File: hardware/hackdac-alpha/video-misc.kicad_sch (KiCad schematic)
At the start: 43 parts, among them J2 TTL SYNC, J3 SYNC OUT, P1 BANK2_AUX, Q1 2N7002, Q2 BC847, Q3 BC857, Q4 BC857, U5 MCP47FEB22A1-E/ST, U6 74LVCH16T245, U7 74LVC1G125, X1 ECS-5032MV-270-CN-TR

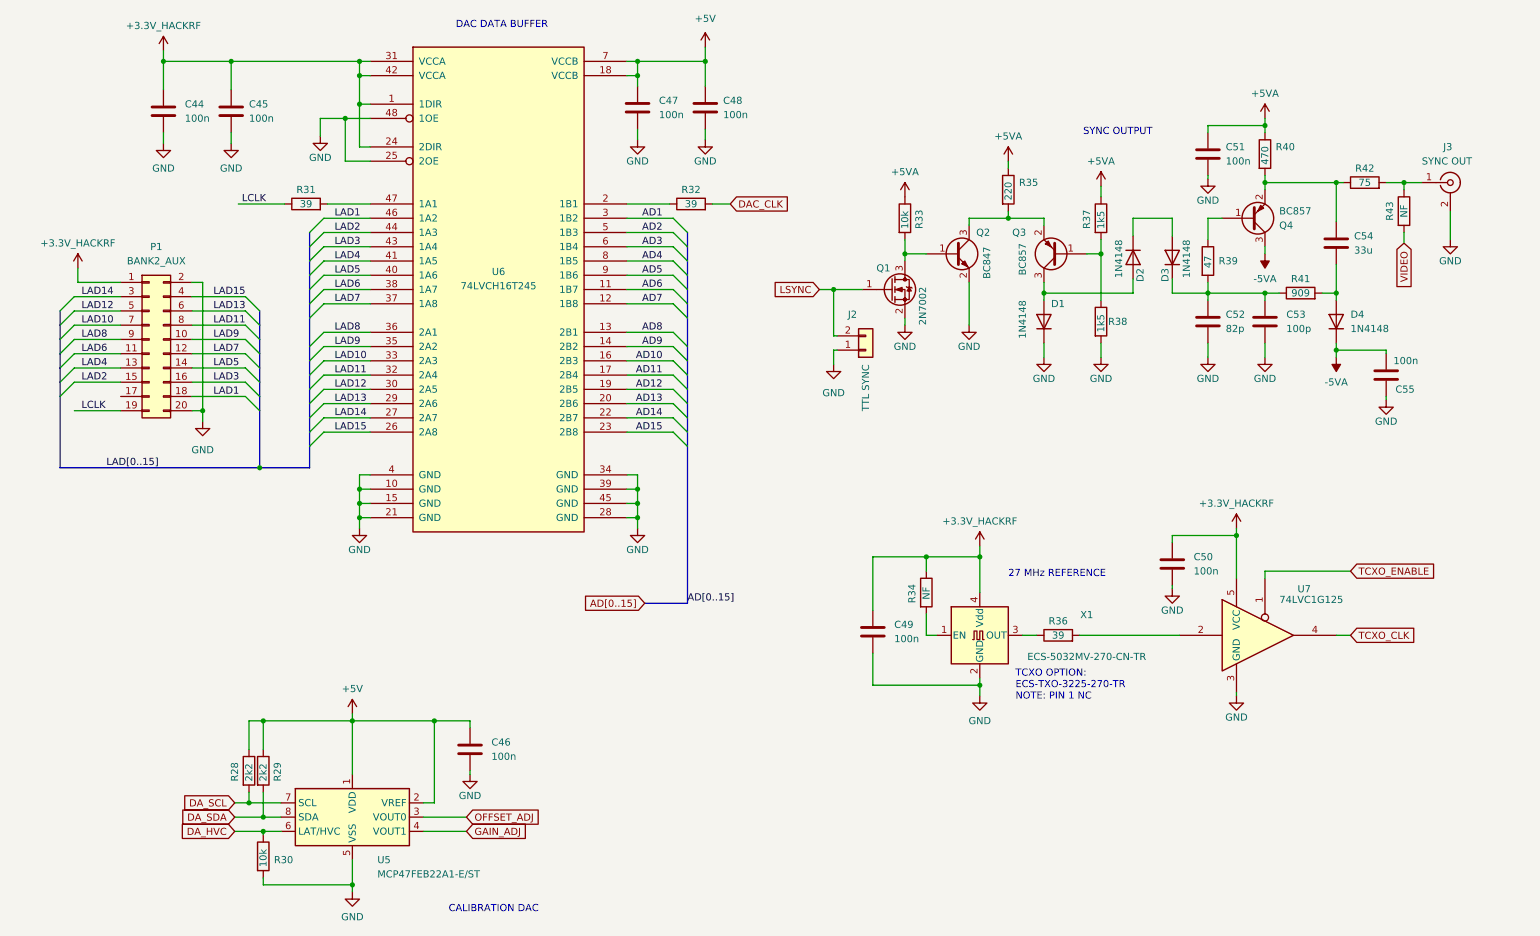
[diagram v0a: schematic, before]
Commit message: Add jumper to configure sync out connector
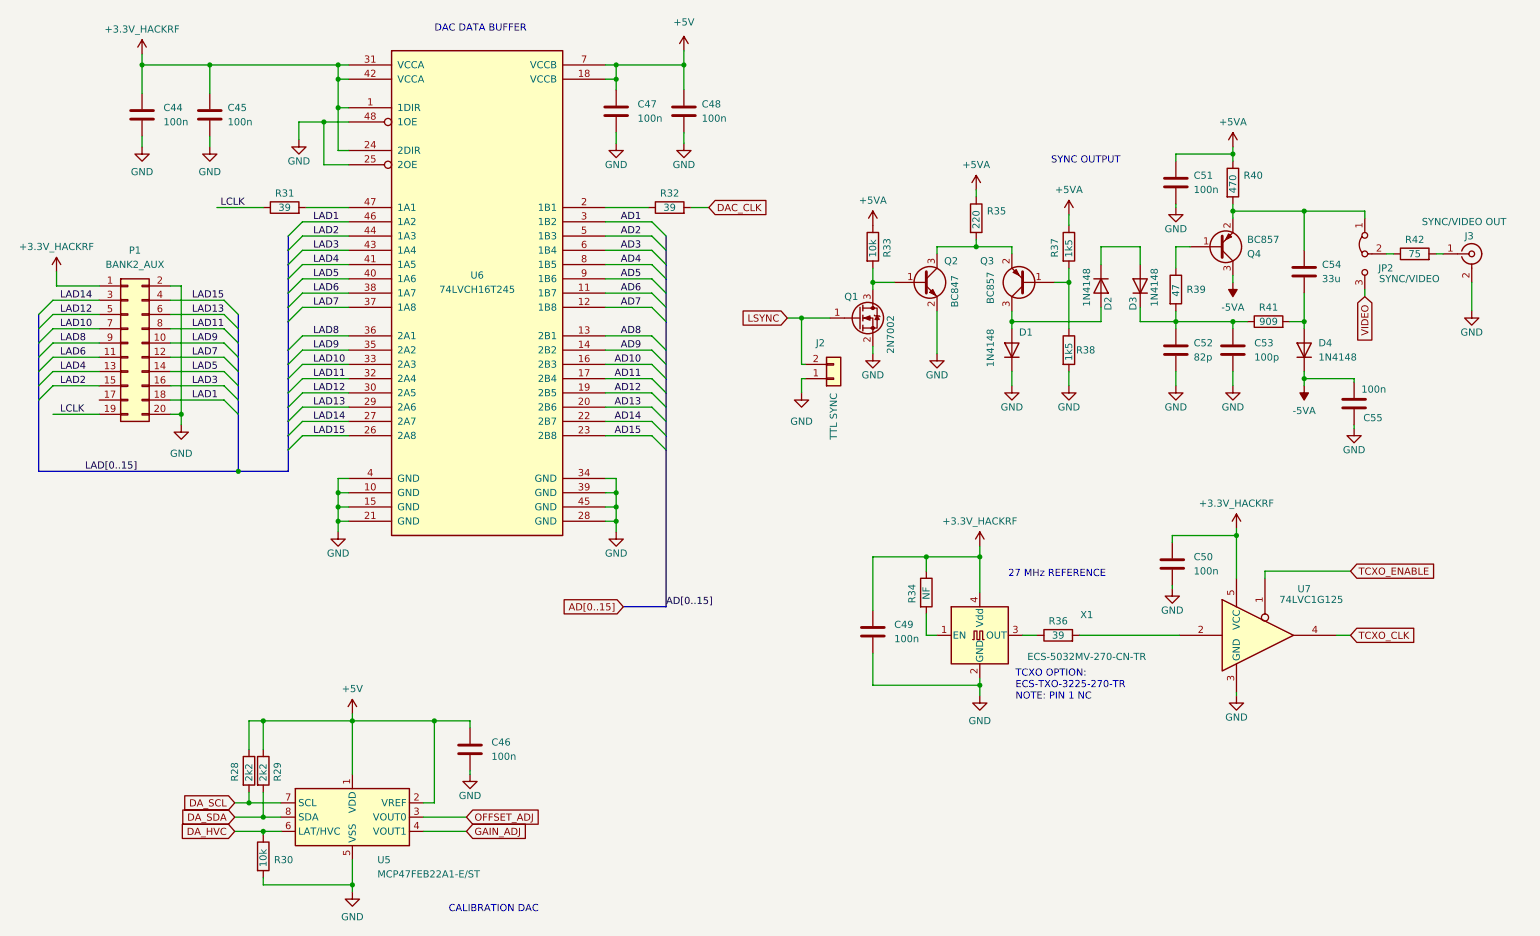
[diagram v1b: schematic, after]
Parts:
- removed R43: NF, Resistor_SMD:R_0603_1608Metric, symbol Device:R
- added JP2: SYNC/VIDEO, Connector_PinHeader_2.54mm:PinHeader_1x03_P2.54mm_Vertical, symbol Jumper:Jumper_3_Bridged12
- J3: value SYNC OUT -> SYNC/VIDEO OUT
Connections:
- net VIDEO: now also JP2.3 (B)
- net at C54.1, Q4.2 (E), R40.2: now also JP2.1 (A); no longer R42.1
- new net: JP2.2 (C), R42.1
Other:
- moved on the sheet: C44, C45, C47, C48, C51, C52, C53, C54, C55, D1, D2, D3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

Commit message: Final V3 board
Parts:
- J3: value SYNC/VIDEO OUT -> VIDEO/SYNC OUT
- JP2: value SYNC/VIDEO -> VIDEO/SYNC
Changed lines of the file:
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@@
 			)
 		)
-		(property "Value" "SYNC/VIDEO OUT"
+		(property "Value" "VIDEO/SYNC OUT"
 			(at 266.065 57.785 0)
 			(effects
@@
 			)
 		)
-		(property "Value" "SYNC/VIDEO"
+		(property "Value" "VIDEO/SYNC"
 			(at 269.24 67.945 90)
 			(effects
